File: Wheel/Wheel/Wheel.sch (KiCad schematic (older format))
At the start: 126 parts, among them J1 Conn_02x09_Odd_Even, J10 RJ45, J11 Screw_Terminal_01x02, J12 DS-201, J13 Conn_01x04, J14 Conn_02x13_Top_Bottom, J15 DB25_Female, J16 Conn_01x06, J17 Conn_01x07, J18 Conn_01x06, J19 RJ45, J2 RJ45, J20 DB9_Male, J21 DB9_Female, J23 Conn_02x15_Odd_Even, J3 RJ45, J4 RJ45, J5 USB_B, J6 Conn_02x10_Odd_Even, J7 Conn_02x09_Odd_Even, J8 RJ45, J9 RJ45, U1 MCP23S17_SP, U10 PC817, U11 IP4220CZ6, U12 PC817, U13 IP4220CZ6, U2 STM32F407VETx, U3 MCP23S17_SP, U4 USBLC6-2SC6, U5 AMS1117, U6 4N35, U7 PC817, U8 PC817, U9 PC817, Y1 32,768 кГц, Y2 8MHz

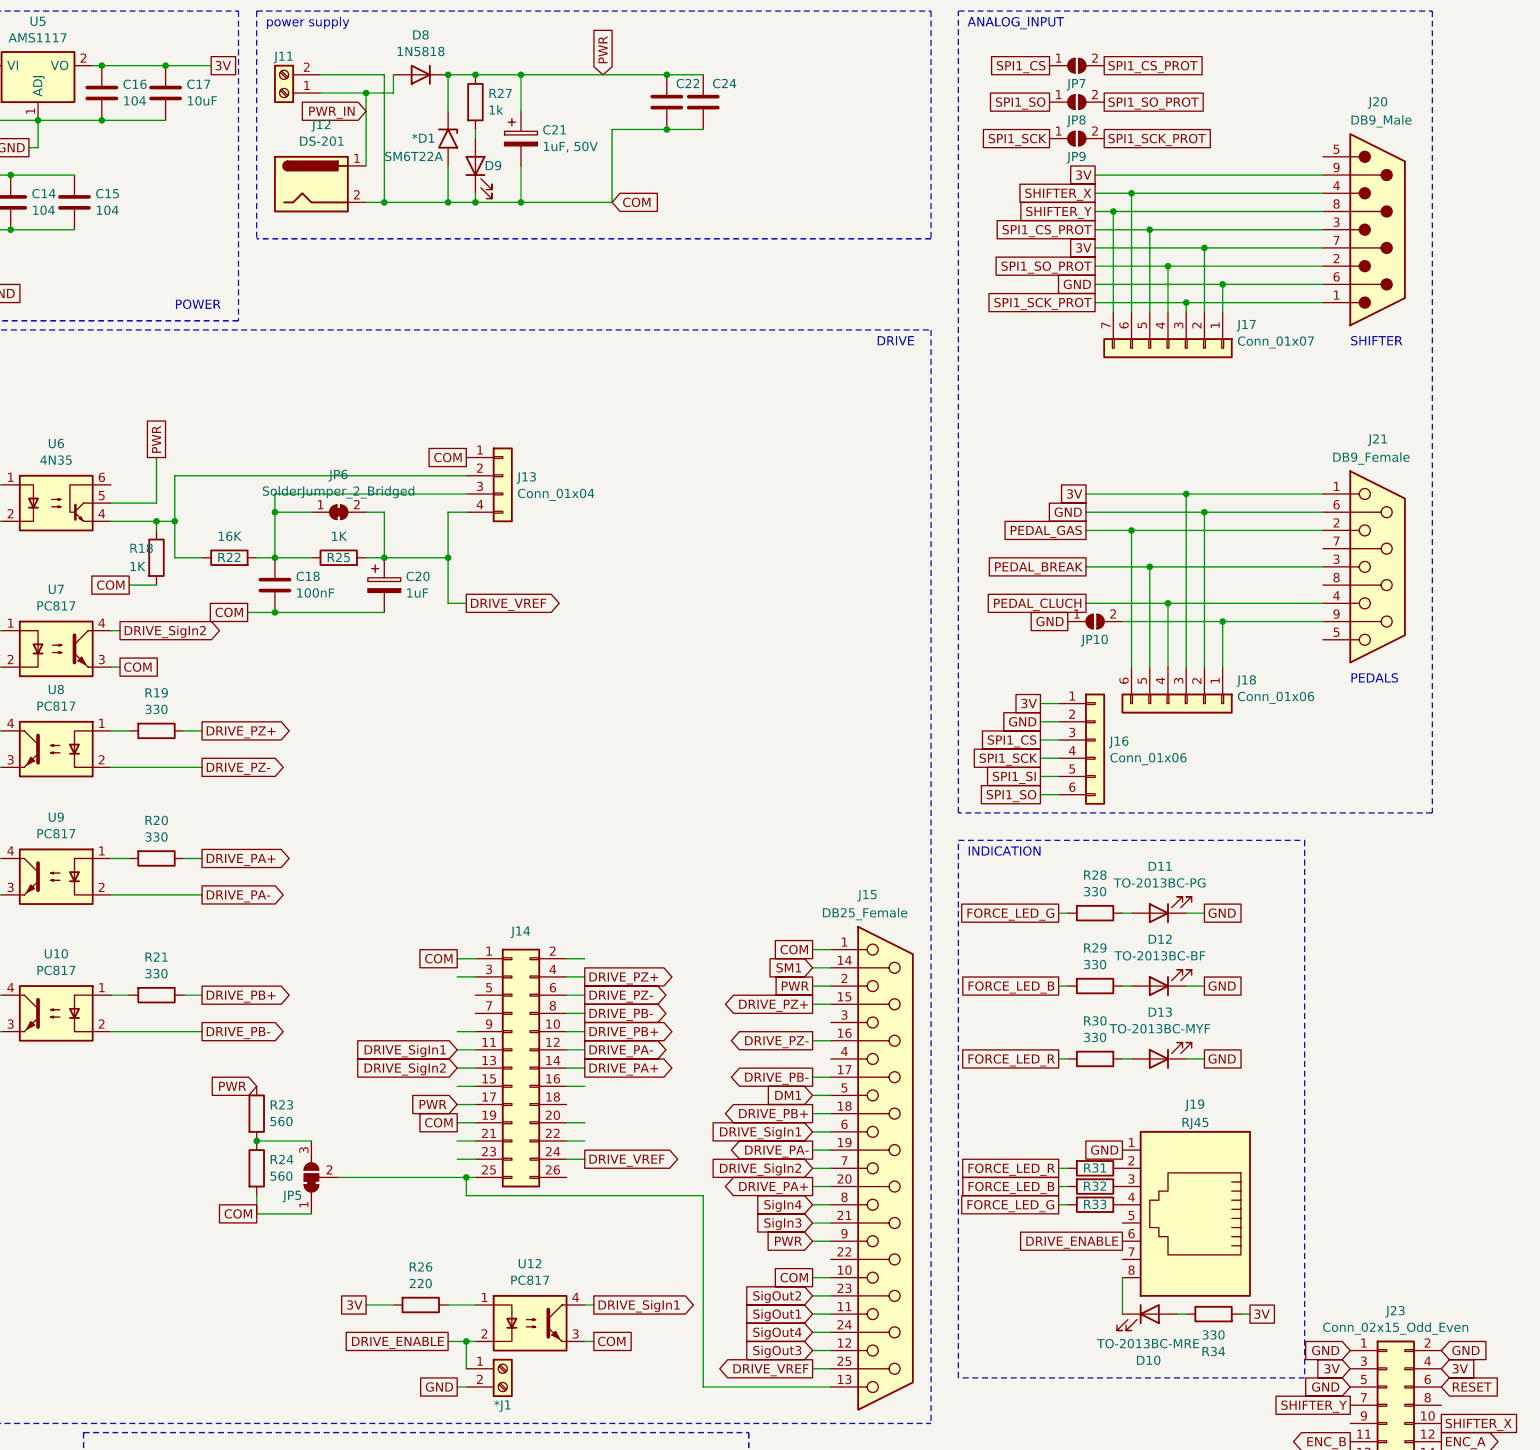
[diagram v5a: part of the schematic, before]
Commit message: Wheel's scheme updated
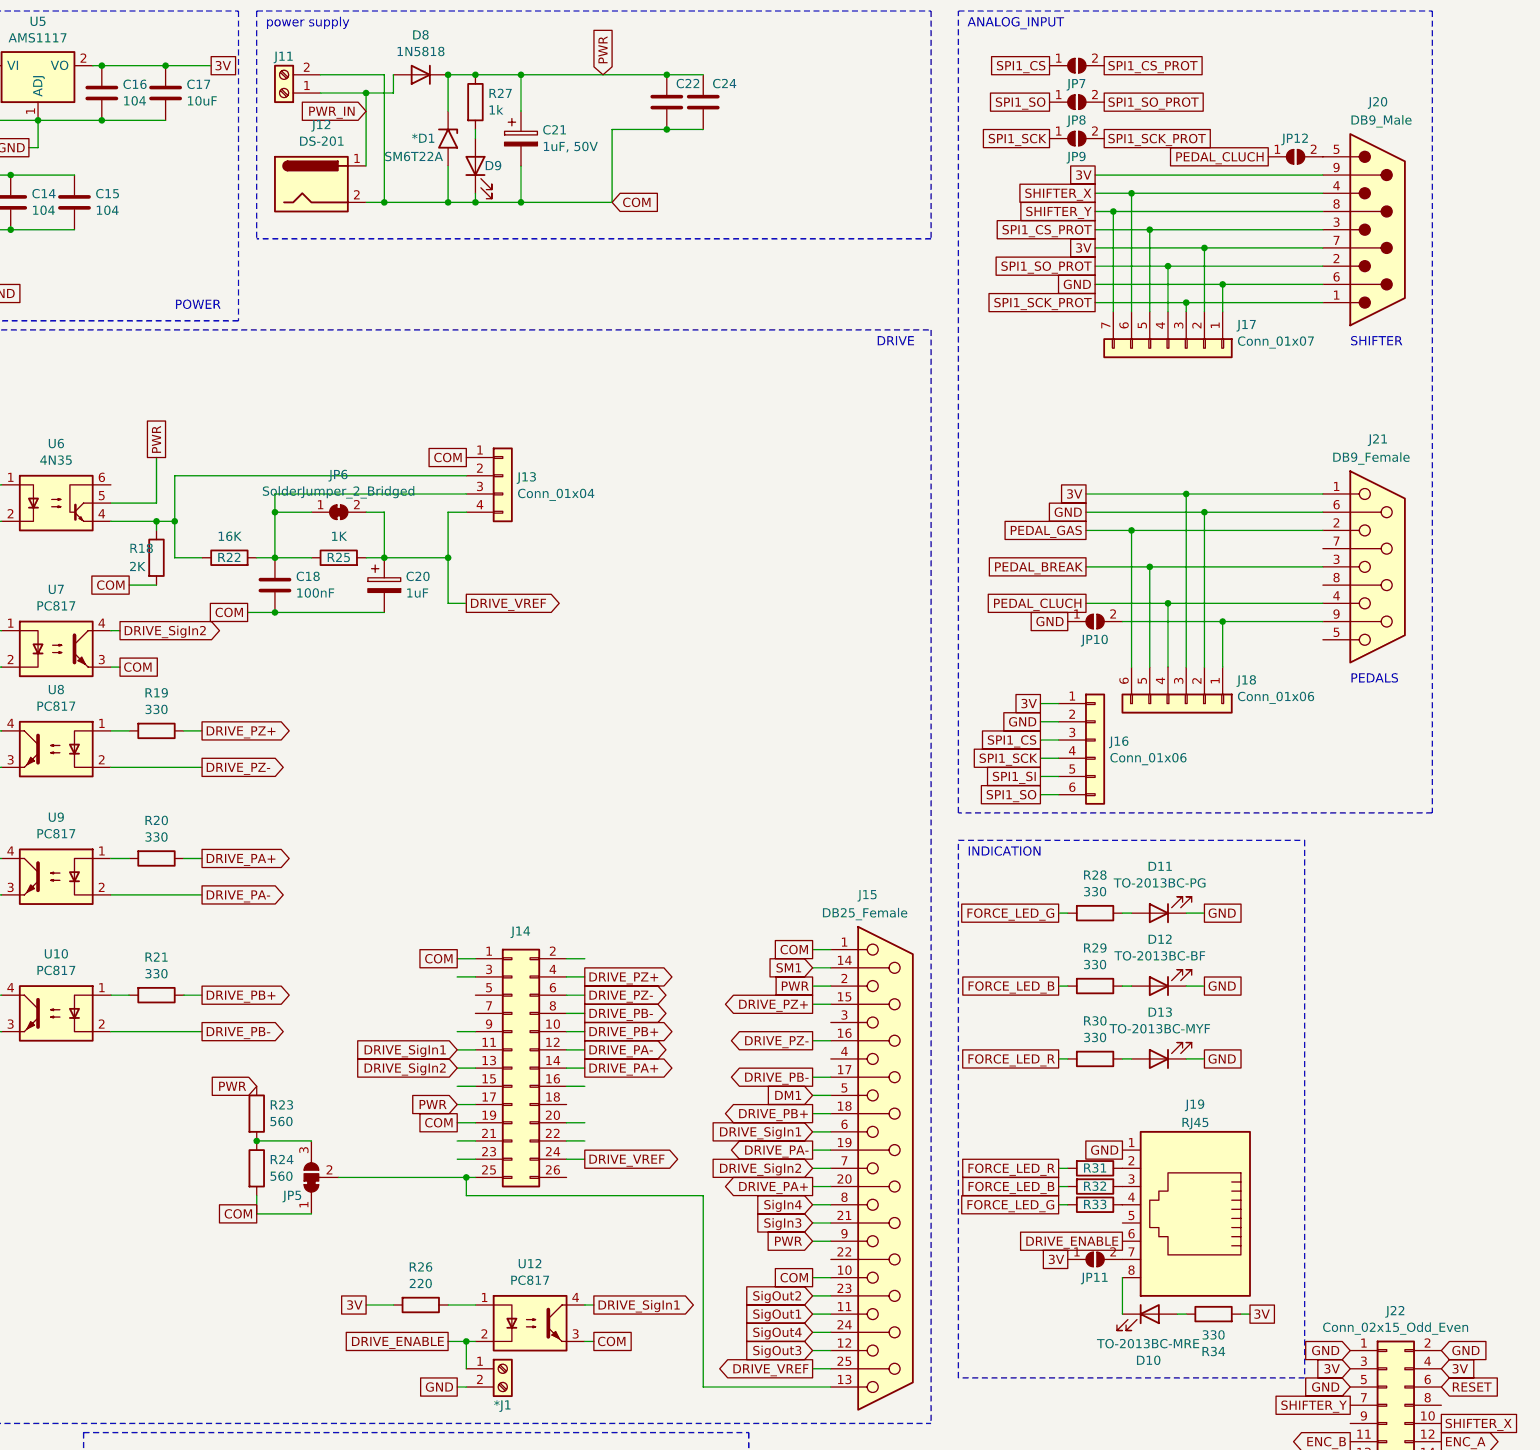
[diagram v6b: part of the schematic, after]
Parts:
- added JP11, JP12: SolderJumper_2_Open, Jumper:SolderJumper-2_P1.3mm_Open_RoundedPad1.0x1.5mm, symbol Jumper:SolderJumper_2_Open
- R18: value 1K -> 2K
- renumbered J23 to J22
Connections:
- net 3V: now also JP11.1 (A)
- net PEDAL_CLUCH: now also JP12.1 (A)
- net at J20.5: now also JP12.2 (B)
- net at J19.7: now also JP11.2 (B)
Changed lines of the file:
@@
 P 8450 3550
 F 0 "R18" H 8300 3600 50  0000 L CNN
-F 1 "1K" H 8300 3500 50  0000 L CNN
+F 1 "2K" H 8300 3500 50  0000 L CNN
 F 2 "Resistor_SMD:R_0805_2012Metric" V 8380 3550 50  0001 C CNN
 F 3 "~" H 8450 3550 50  0001 C CNN
@@
 SPI1_SCK_PROT
 $Comp
-L Connector_Generic:Conn_02x15_Odd_Even J23
+L Connector_Generic:Conn_02x15_Odd_Even J22
 U 1 1 603B8041
 P 15200 8600
-F 0 "J23" H 15250 9517 50  0000 C CNN
+F 0 "J22" H 15250 9517 50  0000 C CNN
 F 1 "Conn_02x15_Odd_Even" H 15250 9426 50  0000 C CNN
 F 2 "Connector_PinHeader_2.54mm:PinHeader_2x15_P2.54mm_Vertical" H 15200 8600 50  0001 C CNN
@@
 Wire Bus Line
 	2650 7500 2650 10500
+$Comp
+L Jumper:SolderJumper_2_Open JP11
+U 1 1 600C876D
+P 13600 7400
+F 0 "JP11" H 13600 7300 50  0000 C CNN
+F 1 "SolderJumper_2_Open" H 13600 7514 50  0001 C CNN
+F 2 "Jumper:SolderJumper-2_P1.3mm_Open_RoundedPad1.0x1.5mm" H 13600 7400 50  0001 C CNN
+F 3 "~" H 13600 7400 50  0001 C CNN
+	1    13600 7400
+	1    0    0    -1
+$EndComp
+Text GLabel 13450 7400 0    50   UnSpc ~ 0
+3V
+$Comp
+L Jumper:SolderJumper_2_Open JP12
+U 1 1 600CA850
+P 14700 1350
+F 0 "JP12" H 14700 1450 50  0000 C CNN
+F 1 "SolderJumper_2_Open" H 14700 1464 50  0001 C CNN
+F 2 "Jumper:SolderJumper-2_P1.3mm_Open_RoundedPad1.0x1.5mm" H 14700 1350 50  0001 C CNN
+F 3 "~" H 14700 1350 50  0001 C CNN
+	1    14700 1350
+	1    0    0    -1
+$EndComp
+Text GLabel 14550 1350 0    50   UnSpc ~ 0
+PEDAL_CLUCH
 $EndSCHEMATC

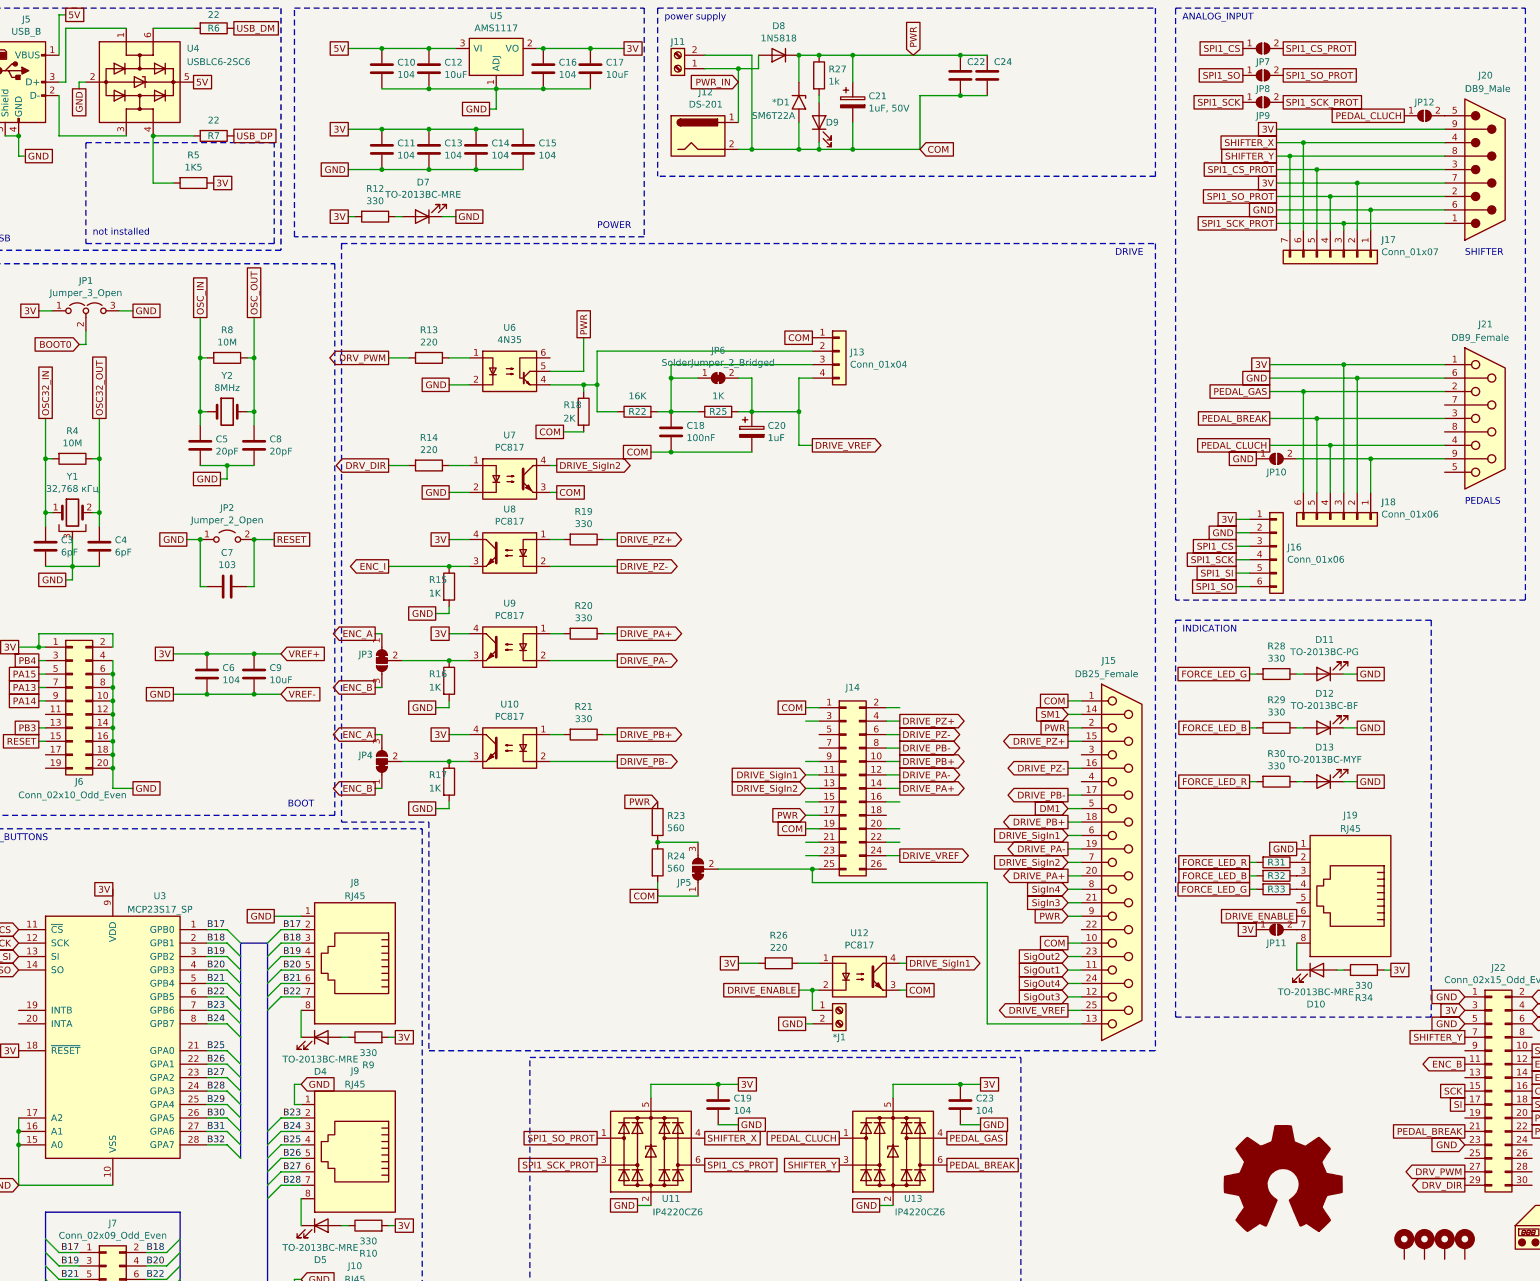
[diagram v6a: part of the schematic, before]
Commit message: I've added rear button for logitech h shifter
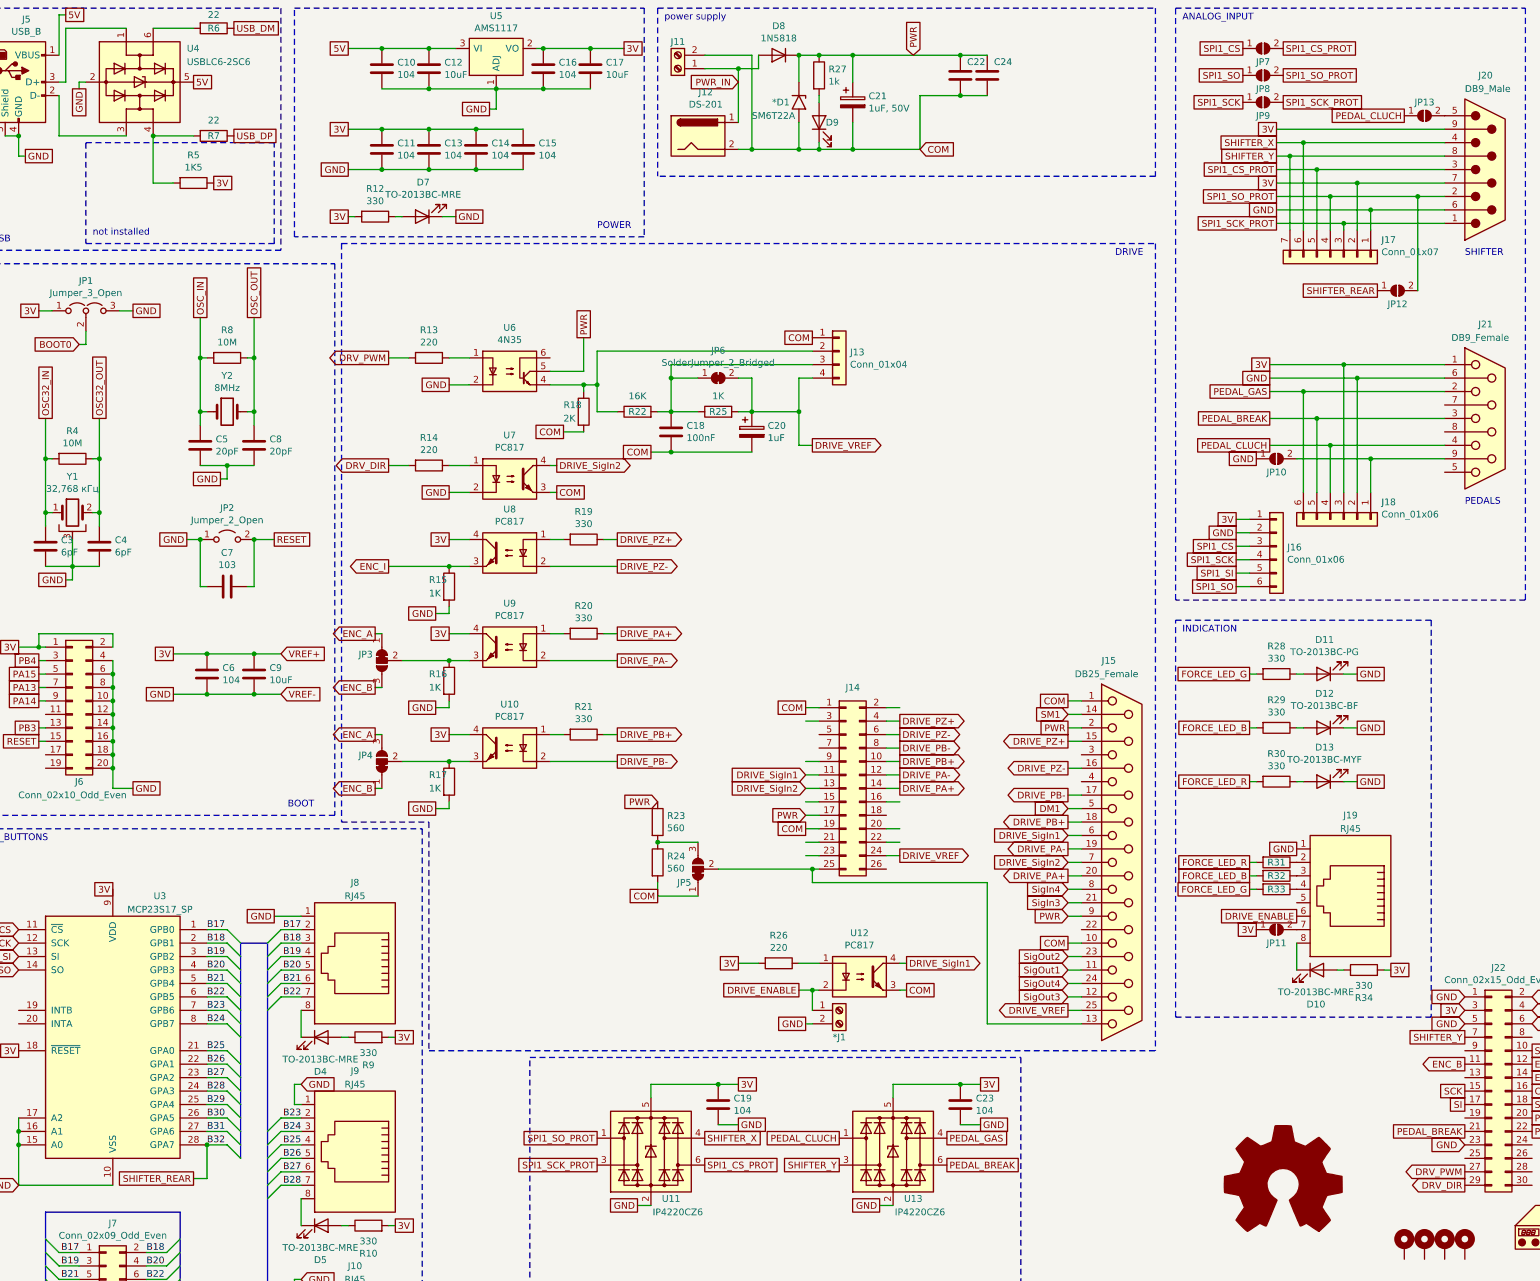
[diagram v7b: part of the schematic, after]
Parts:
- added JP12: SolderJumper_2_Open, Jumper:SolderJumper-2_P1.3mm_Open_RoundedPad1.0x1.5mm, symbol Jumper:SolderJumper_2_Open
- renumbered JP12 to JP13
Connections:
- net SPI1_SO_PROT: now also JP12.2 (B)
- net B32 renamed SHIFTER_REAR
- net SHIFTER_REAR: now also JP12.1 (A)
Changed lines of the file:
@@
 	2200 8900 2350 8900
-Wire Wire Line
-	2200 9000 2350 9000
 Wire Wire Line
 	2750 7400 2900 7400
@@
 F 1 "DB9_Female" H 14900 4200 50  0000 L CNN
 F 2 "Connector_Dsub:DSUB-9_Female_Horizontal_P2.77x2.84mm_EdgePinOffset7.70mm_Housed_MountingHolesOffset9.12mm" H 15150 3600 50  0001 C CNN
-F 3 " ~" H 15150 3600 50  0001 C CNN
+F 3 "https://www.chipdip.ru/product/drb-9fa" H 15150 3600 50  0001 C CNN
 	1    15150 3600
 	1    0    0    -1
@@
 	14100 2150 14850 2150
 Wire Wire Line
-	14000 1950 14850 1950
+	14000 1950 14650 1950
 Wire Wire Line
 	13900 1750 14850 1750
@@
 	1    0    0    -1
 $EndComp
+$Comp
+L Jumper:SolderJumper_2_Open JP11
+U 1 1 600C876D
+P 13600 7400
+F 0 "JP11" H 13600 7300 50  0000 C CNN
+F 1 "SolderJumper_2_Open" H 13600 7514 50  0001 C CNN
+F 2 "Jumper:SolderJumper-2_P1.3mm_Open_RoundedPad1.0x1.5mm" H 13600 7400 50  0001 C CNN
+F 3 "~" H 13600 7400 50  0001 C CNN
+	1    13600 7400
+	1    0    0    -1
+$EndComp
+Text GLabel 13450 7400 0    50   UnSpc ~ 0
+3V
+$Comp
+L Jumper:SolderJumper_2_Open JP13
+U 1 1 600CA850
+P 14700 1350
+F 0 "JP13" H 14700 1450 50  0000 C CNN
+F 1 "SolderJumper_2_Open" H 14700 1464 50  0001 C CNN
+F 2 "Jumper:SolderJumper-2_P1.3mm_Open_RoundedPad1.0x1.5mm" H 14700 1350 50  0001 C CNN
+F 3 "~" H 14700 1350 50  0001 C CNN
+	1    14700 1350
+	1    0    0    -1
+$EndComp
+Text GLabel 14550 1350 0    50   UnSpc ~ 0
+PEDAL_CLUCH
+$Comp
+L Jumper:SolderJumper_2_Open JP12
+U 1 1 6019891C
+P 14500 2650
+F 0 "JP12" H 14500 2550 50  0000 C CNN
+F 1 "SolderJumper_2_Open" H 14500 2764 50  0001 C CNN
+F 2 "Jumper:SolderJumper-2_P1.3mm_Open_RoundedPad1.0x1.5mm" H 14500 2650 50  0001 C CNN
+F 3 "~" H 14500 2650 50  0001 C CNN
+	1    14500 2650
+	1    0    0    -1
+$EndComp
+Wire Wire Line
+	14650 2650 14650 1950
+Connection ~ 14650 1950
+Wire Wire Line
+	14650 1950 14850 1950
+Text GLabel 14350 2650 0    50   UnSpc ~ 0
+SHIFTER_REAR
+Text GLabel 5550 9250 0    50   UnSpc ~ 0
+SHIFTER_REAR
+Wire Wire Line
+	2200 9000 2350 9000
+Wire Wire Line
+	5550 9250 5650 9250
+Wire Wire Line
+	5650 9250 5650 9000
 Wire Bus Line
 	4450 9500 4450 10400
@@
 Wire Bus Line
 	2650 7500 2650 10500
-$Comp
-L Jumper:SolderJumper_2_Open JP11
-U 1 1 600C876D
-P 13600 7400
-F 0 "JP11" H 13600 7300 50  0000 C CNN
-F 1 "SolderJumper_2_Open" H 13600 7514 50  0001 C CNN
-F 2 "Jumper:SolderJumper-2_P1.3mm_Open_RoundedPad1.0x1.5mm" H 13600 7400 50  0001 C CNN
-F 3 "~" H 13600 7400 50  0001 C CNN
-	1    13600 7400
-	1    0    0    -1
-$EndComp
-Text GLabel 13450 7400 0    50   UnSpc ~ 0
-3V
-$Comp
-L Jumper:SolderJumper_2_Open JP12
-U 1 1 600CA850
-P 14700 1350
-F 0 "JP12" H 14700 1450 50  0000 C CNN
-F 1 "SolderJumper_2_Open" H 14700 1464 50  0001 C CNN
-F 2 "Jumper:SolderJumper-2_P1.3mm_Open_RoundedPad1.0x1.5mm" H 14700 1350 50  0001 C CNN
-F 3 "~" H 14700 1350 50  0001 C CNN
-	1    14700 1350
-	1    0    0    -1
-$EndComp
-Text GLabel 14550 1350 0    50   UnSpc ~ 0
-PEDAL_CLUCH
+Connection ~ 5650 9000
 $EndSCHEMATC
